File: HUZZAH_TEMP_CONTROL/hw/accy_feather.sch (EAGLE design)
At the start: 26 parts

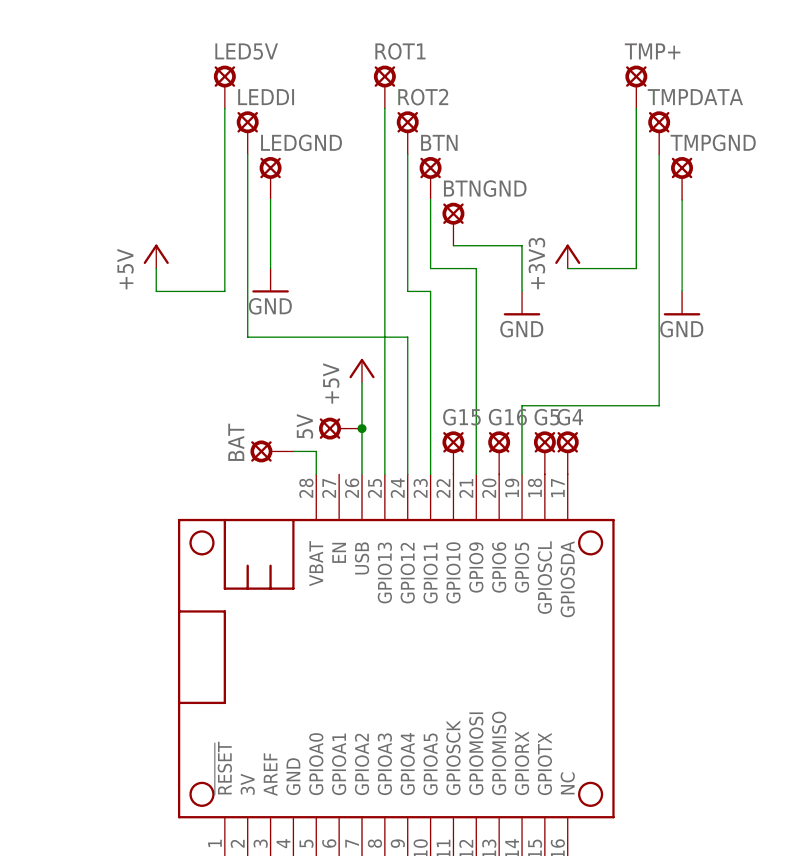
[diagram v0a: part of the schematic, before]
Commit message: Update feather accy board to v1.1
Added 4.7k pullup on temp data line
Added level shifter on LED data line 3.3v->5V
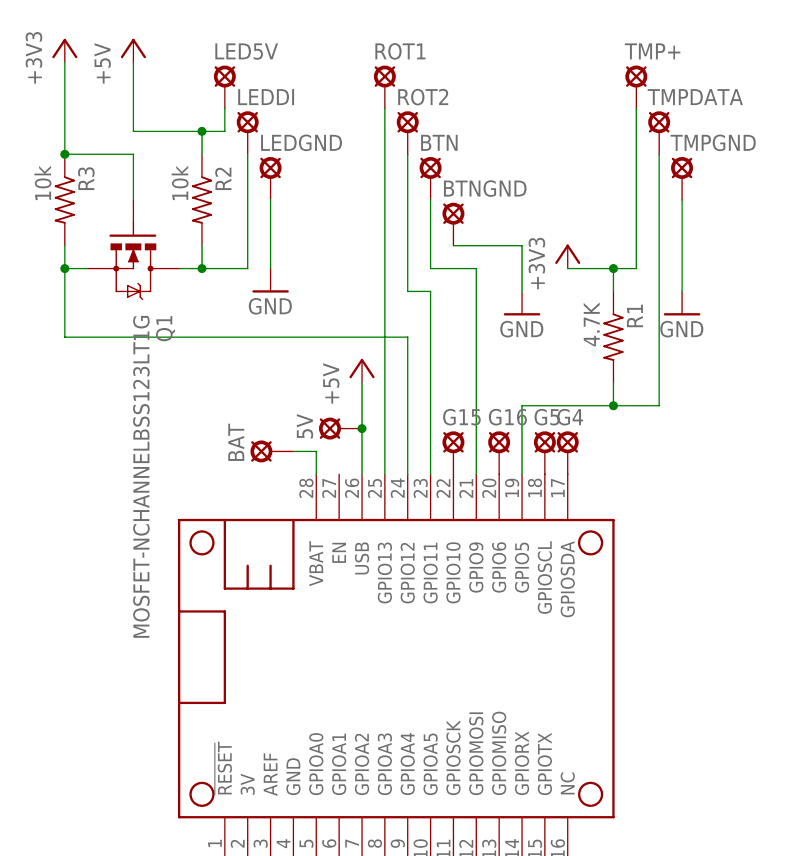
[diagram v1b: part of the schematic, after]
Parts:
- added Q1: MOSFET-NCHANNELBSS123LT1G, SparkFun-DiscreteSemi:MOSFET-NCHANNELBSS123LT1G
- added R1: 4.7K, resistor:R-US_R0603
- added R2, R3: 10k, resistor:R-US_R0603
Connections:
- removed net +3V3: 3V.MP, MS1.3V, TMP+.MP
- new net N$18: LEDDI.MP, Q1.D, R2.2
- new net N$19: MS1.GPIO12, Q1.S, R3.2
- net +5V: now also R2.1
- net N$1: now also R1.2
- net N$6: now also 3V.MP, MS1.3V, Q1.G, R1.1, R3.1, TMP+.MP; no longer LEDDI.MP, MS1.GPIO12
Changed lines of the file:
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@@
 <part name="BAT" library="solpad" deviceset="SE11" device=""/>
 <part name="FRAME1" library="frames" deviceset="LETTER_L" device=""/>
+<part name="R1" library="resistor" deviceset="R-US_" device="R0603" value="4.7K"/>
+<part name="Q1" library="SparkFun-DiscreteSemi" deviceset="MOSFET-NCHANNEL" device="BSS123LT1G"/>
+<part name="R2" library="resistor" deviceset="R-US_" device="R0603" value="10k"/>
+<part name="R3" library="resistor" deviceset="R-US_" device="R0603" value="10k"/>
+<part name="+3V3" library="supply1" deviceset="+3V3" device=""/>
 </parts>
 <sheets>
@@
 <instance part="+3V2" gate="G$1" x="119.38" y="109.22"/>
 <instance part="GND3" gate="1" x="114.3" y="101.6"/>
-<instance part="P+2" gate="1" x="73.66" y="109.22"/>
+<instance part="P+2" gate="1" x="71.12" y="132.08"/>
 <instance part="GND4" gate="1" x="86.36" y="104.14"/>
 <instance part="LED5V" gate="1" x="81.28" y="127"/>
@@
 <instance part="FRAME1" gate="G$1" x="0" y="0"/>
 <instance part="FRAME1" gate="G$2" x="147.32" y="0"/>
+<instance part="R1" gate="G$1" x="124.46" y="99.06" rot="R270"/>
+<instance part="Q1" gate="G$1" x="71.12" y="106.68" rot="R270"/>
+<instance part="R2" gate="G$1" x="78.74" y="114.3" rot="R270"/>
+<instance part="R3" gate="G$1" x="63.5" y="114.3" rot="R270"/>
+<instance part="+3V3" gate="G$1" x="63.5" y="132.08"/>
 </instances>
 <busses>
@@
 </segment>
 <segment>
-<wire x1="81.28" y1="124.46" x2="81.28" y2="104.14" width="0.1524" layer="91"/>
-<wire x1="81.28" y1="104.14" x2="73.66" y2="104.14" width="0.1524" layer="91"/>
+<wire x1="81.28" y1="124.46" x2="81.28" y2="121.92" width="0.1524" layer="91"/>
+<wire x1="81.28" y1="121.92" x2="78.74" y2="121.92" width="0.1524" layer="91"/>
 <pinref part="P+2" gate="1" pin="+5V"/>
-<wire x1="73.66" y1="104.14" x2="73.66" y2="106.68" width="0.1524" layer="91"/>
+<wire x1="78.74" y1="121.92" x2="71.12" y2="121.92" width="0.1524" layer="91"/>
+<wire x1="71.12" y1="121.92" x2="71.12" y2="129.54" width="0.1524" layer="91"/>
 <pinref part="LED5V" gate="1" pin="MP"/>
-</segment>
-</net>
-<net name="+3V3" class="0">
+<pinref part="R2" gate="G$1" pin="1"/>
+<wire x1="78.74" y1="119.38" x2="78.74" y2="121.92" width="0.1524" layer="91"/>
+<junction x="78.74" y="121.92"/>
+</segment>
+</net>
+<net name="N$6" class="0">
 <segment>
 <pinref part="MS1" gate="G$1" pin="3V"/>
@@
 <segment>
 <wire x1="127" y1="124.46" x2="127" y2="106.68" width="0.1524" layer="91"/>
-<wire x1="127" y1="106.68" x2="119.38" y2="106.68" width="0.1524" layer="91"/>
+<wire x1="127" y1="106.68" x2="124.46" y2="106.68" width="0.1524" layer="91"/>
 <pinref part="+3V2" gate="G$1" pin="+3V3"/>
 <pinref part="TMP+" gate="1" pin="MP"/>
+<pinref part="R1" gate="G$1" pin="1"/>
+<wire x1="124.46" y1="106.68" x2="119.38" y2="106.68" width="0.1524" layer="91"/>
+<wire x1="124.46" y1="104.14" x2="124.46" y2="106.68" width="0.1524" layer="91"/>
+<junction x="124.46" y="106.68"/>
+</segment>
+<segment>
+<pinref part="+3V3" gate="G$1" pin="+3V3"/>
+<pinref part="R3" gate="G$1" pin="1"/>
+<wire x1="63.5" y1="129.54" x2="63.5" y2="119.38" width="0.1524" layer="91"/>
+<pinref part="Q1" gate="G$1" pin="G"/>
+<wire x1="63.5" y1="119.38" x2="71.12" y2="119.38" width="0.1524" layer="91"/>
+<wire x1="71.12" y1="119.38" x2="71.12" y2="114.3" width="0.1524" layer="91"/>
+<junction x="63.5" y="119.38"/>
 </segment>
 </net>
@@
 <wire x1="129.54" y1="91.44" x2="129.54" y2="119.38" width="0.1524" layer="91"/>
 <wire x1="114.3" y1="83.82" x2="114.3" y2="91.44" width="0.1524" layer="91"/>
-<wire x1="114.3" y1="91.44" x2="129.54" y2="91.44" width="0.1524" layer="91"/>
+<wire x1="114.3" y1="91.44" x2="124.46" y2="91.44" width="0.1524" layer="91"/>
 <pinref part="TMPDATA" gate="1" pin="MP"/>
+<pinref part="R1" gate="G$1" pin="2"/>
+<wire x1="124.46" y1="91.44" x2="129.54" y2="91.44" width="0.1524" layer="91"/>
+<wire x1="124.46" y1="91.44" x2="124.46" y2="93.98" width="0.1524" layer="91"/>
+<junction x="124.46" y="91.44"/>
 </segment>
 </net>
@@
 </segment>
 </net>
-<net name="N$6" class="0">
-<segment>
-<pinref part="MS1" gate="G$1" pin="GPIO12"/>
-<wire x1="101.6" y1="83.82" x2="101.6" y2="99.06" width="0.1524" layer="91"/>
-<wire x1="101.6" y1="99.06" x2="83.82" y2="99.06" width="0.1524" layer="91"/>
-<wire x1="83.82" y1="99.06" x2="83.82" y2="119.38" width="0.1524" layer="91"/>
-<pinref part="LEDDI" gate="1" pin="MP"/>
-</segment>
-</net>
 <net name="N$4" class="0">
 <segment>
@@
 </segment>
 </net>
+<net name="N$18" class="0">
+<segment>
+<pinref part="Q1" gate="G$1" pin="D"/>
+<wire x1="76.2" y1="106.68" x2="78.74" y2="106.68" width="0.1524" layer="91"/>
+<pinref part="R2" gate="G$1" pin="2"/>
+<wire x1="78.74" y1="106.68" x2="78.74" y2="109.22" width="0.1524" layer="91"/>
+<wire x1="78.74" y1="106.68" x2="83.82" y2="106.68" width="0.1524" layer="91"/>
+<wire x1="83.82" y1="106.68" x2="83.82" y2="119.38" width="0.1524" layer="91"/>
+<pinref part="LEDDI" gate="1" pin="MP"/>
+<junction x="78.74" y="106.68"/>
+</segment>
+</net>
+<net name="N$19" class="0">
+<segment>
+<pinref part="MS1" gate="G$1" pin="GPIO12"/>
+<wire x1="101.6" y1="83.82" x2="101.6" y2="99.06" width="0.1524" layer="91"/>
+<wire x1="101.6" y1="99.06" x2="63.5" y2="99.06" width="0.1524" layer="91"/>
+<pinref part="Q1" gate="G$1" pin="S"/>
+<wire x1="66.04" y1="106.68" x2="63.5" y2="106.68" width="0.1524" layer="91"/>
+<pinref part="R3" gate="G$1" pin="2"/>
+<wire x1="63.5" y1="106.68" x2="63.5" y2="109.22" width="0.1524" layer="91"/>
+<wire x1="63.5" y1="99.06" x2="63.5" y2="106.68" width="0.1524" layer="91"/>
+<junction x="63.5" y="106.68"/>
+</segment>
+</net>

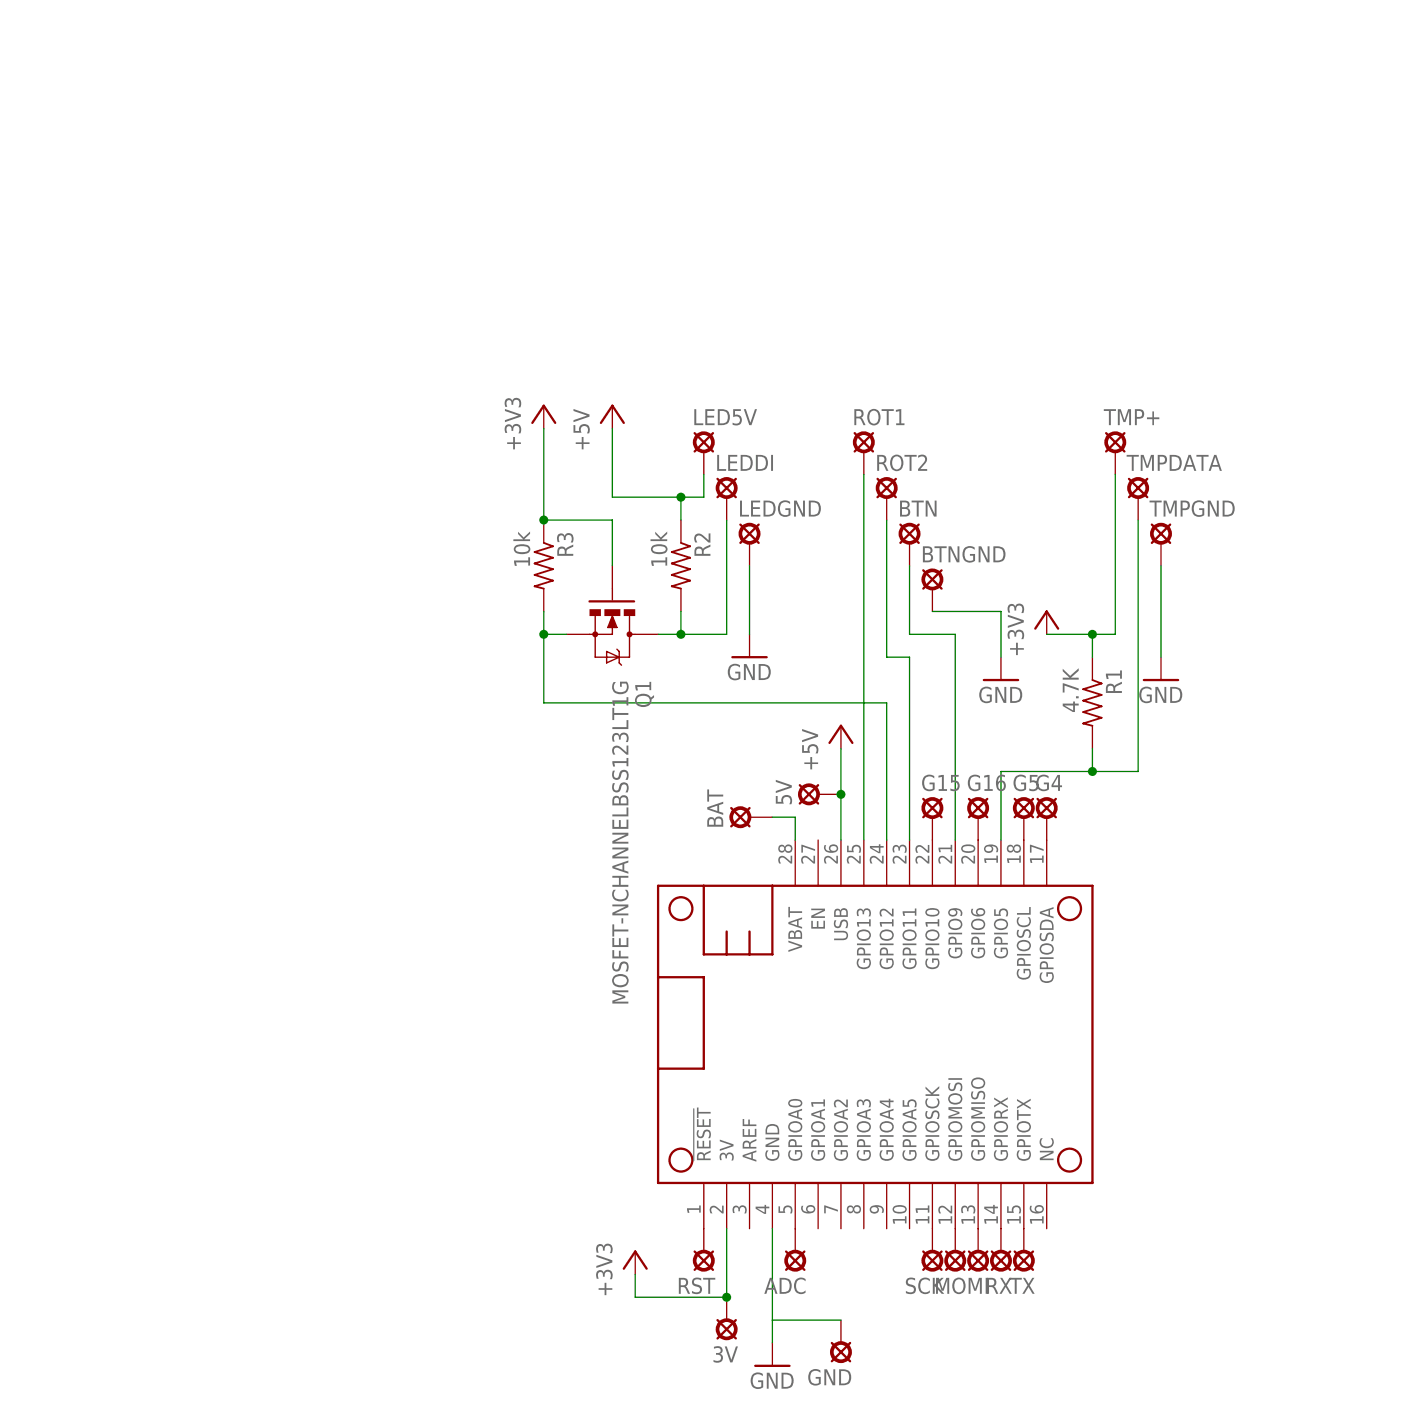
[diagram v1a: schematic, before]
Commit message: Accessory board version 1.2
Removed the MOSFET based level shifter for LED data and replaced
it with a TI TXS01012.  The MOSFET level shifter worked, but it
wasn't fast enough to keep good data integrity for the WS2811 LED
driver.

I also routed the relay control through the same TXS01012 level
shifter so it can be safely used to drive an external SSR instead
of a feather relay board.
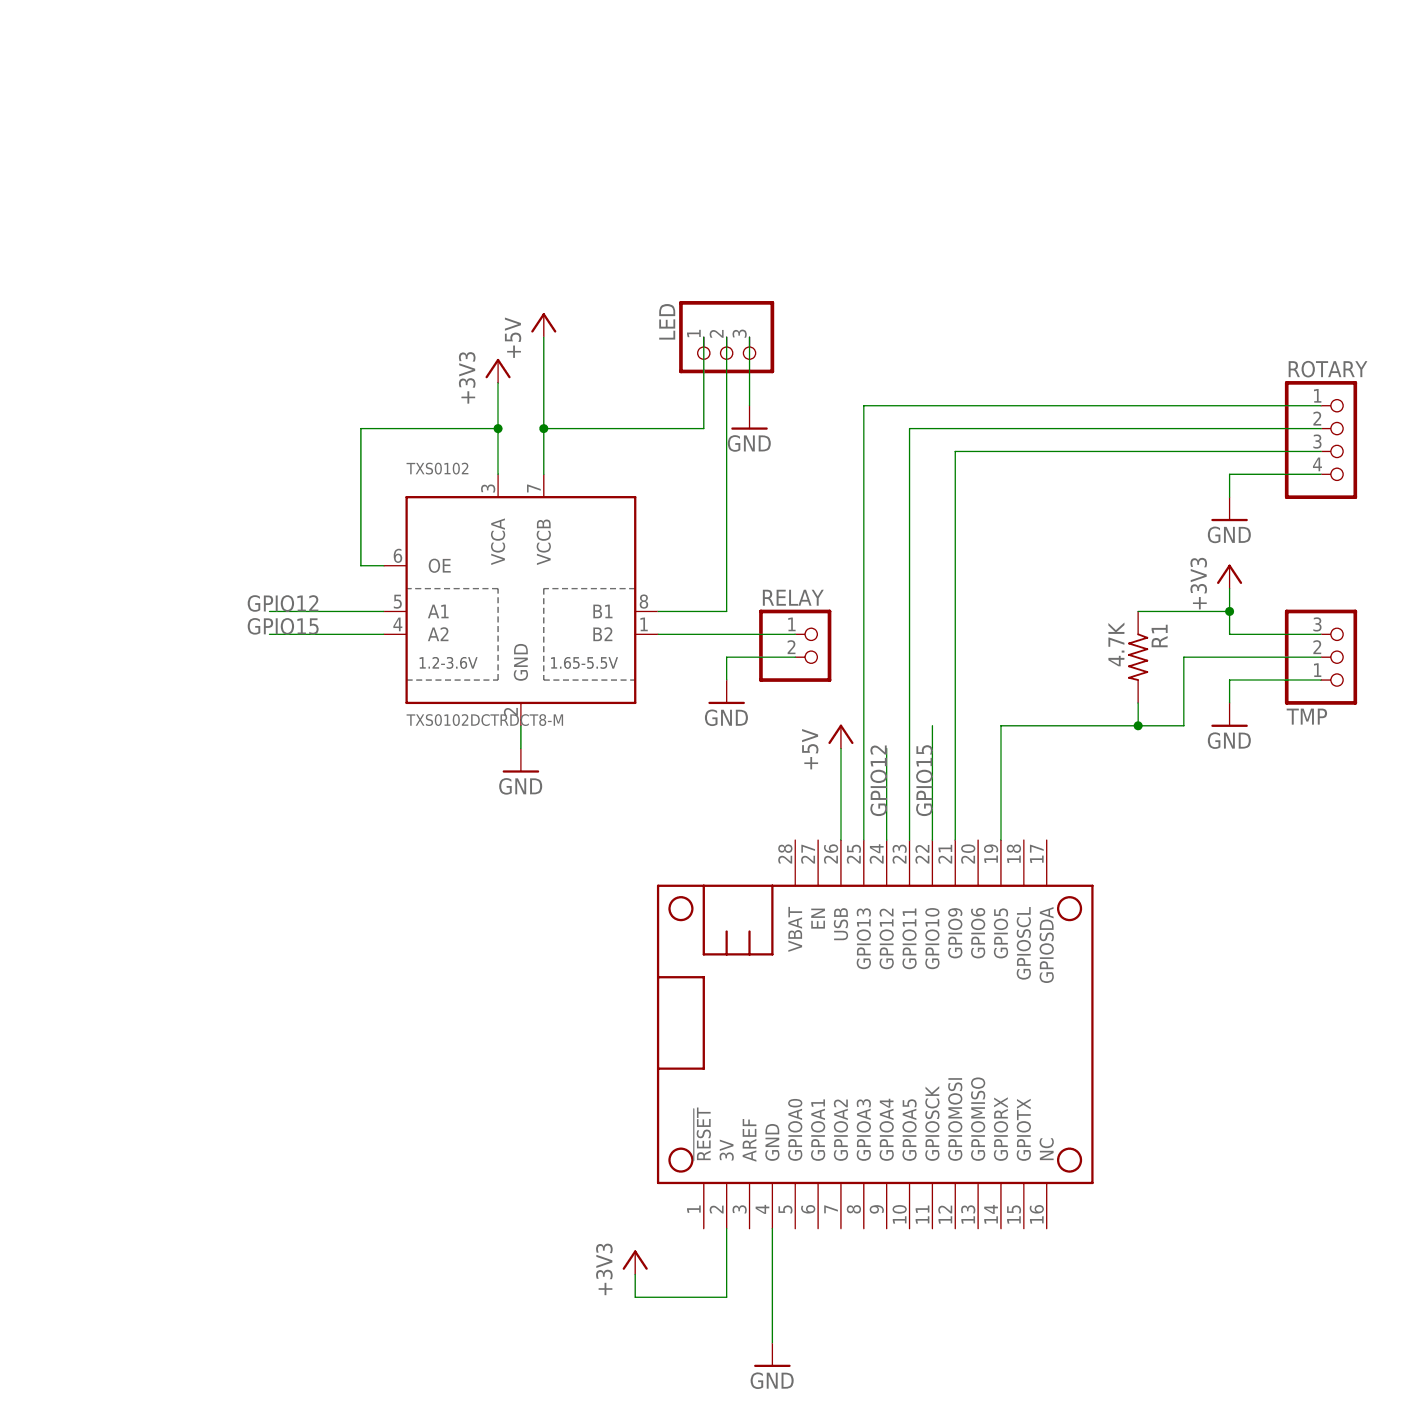
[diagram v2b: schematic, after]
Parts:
- removed 3V, 5V, ADC, BAT, BTN, BTNGND, G15, G16, G4, G5, GND, LED5V, LEDDI, LEDGND, MI, MO, ROT1, ROT2, RST, RX, SCK, TMP+, TMPDATA, TMPGND, TX: SE11, solpad:SE11
- removed Q1: MOSFET-NCHANNELBSS123LT1G, SparkFun-DiscreteSemi:MOSFET-NCHANNELBSS123LT1G
- removed R2, R3: 10k, resistor:R-US_R0603
- added LED, TMP: (no value), adafruit:PINHD-1X3CB
- added RELAY: (no value), pinhead:PINHD-1X2
- added ROTARY: (no value), pinhead:PINHD-1X4
- added TXS0102: TXS0102DCTRDCT8-M, DZ:TXS0102DCTRDCT8-M
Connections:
- removed net N$1: MS1.GPIO5, R1.2, TMPDATA.MP
- removed net N$10: MS1.GPIOSCK, SCK.MP
- removed net N$11: ADC.MP, MS1.GPIOA0
- removed net N$12: MO.MP, MS1.GPIOMOSI
- removed net N$13: MI.MP, MS1.GPIOMISO
- removed net N$14: MS1.GPIORX, RX.MP
- removed net N$15: MS1.GPIOTX, TX.MP
- removed net N$18: LEDDI.MP, Q1.D, R2.2
- removed net N$19: MS1.GPIO12, Q1.S, R3.2
- removed net N$2: BTN.MP, MS1.GPIO9
- removed net N$3: MS1.GPIO11, ROT2.MP
- removed net N$4: G4.MP, MS1.GPIOSDA
- removed net N$5: G5.MP, MS1.GPIOSCL
- removed net N$6: 3V.MP, MS1.3V, Q1.G, R1.1, R3.1, TMP+.MP
- removed net N$7: G16.MP, MS1.GPIO6
- removed net N$8: G15.MP, MS1.GPIO10
- removed net N$9: MS1.!RESET, RST.MP
- removed net VBAT: BAT.MP, MS1.VBAT
- new net +3V3: MS1.3V, R1.1, TMP.3, TXS0102.OE, TXS0102.VCCA
- new net BTN: MS1.GPIO9, ROTARY.3
- new net GPIO12: MS1.GPIO12, TXS0102.A1
- new net GPIO15: MS1.GPIO10, TXS0102.A2
- new net LED_DATA: LED.2, TXS0102.B1
- new net RELAY: RELAY.1, TXS0102.B2
- new net ROT1: MS1.GPIO13, ROTARY.1
- new net TMP_DATA: MS1.GPIO5, R1.2, TMP.2
- net +5V: now also LED.1, TXS0102.VCCB; no longer 5V.MP, LED5V.MP, R2.1
- net GND: now also LED.3, RELAY.2, ROTARY.4, TMP.1, TXS0102.GND; no longer BTNGND.MP, GND.MP, LEDGND.MP, TMPGND.MP
- net ROT2: now also MS1.GPIO11, ROTARY.2; no longer MS1.GPIO13, ROT1.MP
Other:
- moved on the sheet: R1
